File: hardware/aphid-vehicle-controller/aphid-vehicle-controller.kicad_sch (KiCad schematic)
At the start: 0 parts

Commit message: worked on schematic
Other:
- added sheet Analog (analog.kicad_sch)
- added sheet Digital (digital.kicad_sch)
- added sheet Monitor (monitor.kicad_sch)
- sheet CAN ports: added CAN1_MONITOR_RX, CAN1_MONITOR_TX; removed none
- sheet Connectors ports: added ACC1, ACC2, BRAKE, CONTACTOR_LOWER, CONTACTOR_UPPER, HIGH_SIDE_DRIVE, PRECHARGE; removed none
- sheet MCU ports: added LOWER_CONTACTOR_ENABLE, PRECHARGE_ENABLE, UPPER_CONTACTOR_ENABLE; removed none
- sheet Power ports: added VIN_SENSE; removed none

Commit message: more work on pcb
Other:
- added sheet Reset (reset.kicad_sch)
- sheet Analog ports: added IGNITION, IGNITION_FILTERED; removed none
- sheet Connectors ports: added CRANK, IGNITION; removed none
- sheet Digital ports: added CONTACTOR_LOWER, CONTACTOR_UPPER, IGNITION, LOWER_ENABLE, PRECHARGE, PRECHARGE_ENABLE, UPPER_ENABLE; removed none
- sheet Monitor ports: added ACC1_FILTERED, ACC2_FILTERED, ENABLE_RESET; removed none
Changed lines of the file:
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@@
 	)
 	(sheet
-		(at 185.42 82.55)
-		(size 38.1 36.83)
+		(at 185.42 80.01)
+		(size 38.1 21.59)
 		(fields_autoplaced yes)
 		(stroke
@@
 		)
 		(property "Sheetname" "Digital"
-			(at 185.42 81.8384 0)
+			(at 185.42 79.2984 0)
 			(effects
 				(font
@@
 		)
 		(property "Sheetfile" "digital.kicad_sch"
-			(at 185.42 119.9646 0)
+			(at 185.42 102.1846 0)
 			(effects
 				(font
@@
 		)
 		(pin "HIGH_SIDE_SENSE" output
-			(at 185.42 116.84 180)
+			(at 185.42 97.79 180)
 			(effects
 				(font
@@
 		)
 		(pin "HIGH_SIDE_ENABLE" output
-			(at 185.42 114.3 180)
+			(at 185.42 93.98 180)
+			(effects
+				(font
+					(size 1.27 1.27)
+				)
+				(justify left)
+			)
+		)
+		(pin "IGNITION" input
+			(at 223.52 82.55 0)
+			(effects
+				(font
+					(size 1.27 1.27)
+				)
+				(justify right)
+			)
+		)
+		(pin "PRECHARGE" output
+			(at 223.52 87.63 0)
+			(effects
+				(font
+					(size 1.27 1.27)
+				)
+				(justify right)
+			)
+		)
+		(pin "PRECHARGE_ENABLE" input
+			(at 185.42 82.55 180)
+			(effects
+				(font
+					(size 1.27 1.27)
+				)
+				(justify left)
+			)
+		)
+		(pin "CONTACTOR_LOWER" output
+			(at 223.52 92.71 0)
+			(effects
+				(font
+					(size 1.27 1.27)
+				)
+				(justify right)
+			)
+		)
+		(pin "CONTACTOR_UPPER" output
+			(at 223.52 90.17 0)
+			(effects
+				(font
+					(size 1.27 1.27)
+				)
+				(justify right)
+			)
+		)
+		(pin "UPPER_ENABLE" input
+			(at 185.42 85.09 180)
+			(effects
+				(font
+					(size 1.27 1.27)
+				)
+				(justify left)
+			)
+		)
+		(pin "LOWER_ENABLE" input
+			(at 185.42 87.63 180)
 			(effects
 				(font
@@
 				(path "/1bdad060-e59b-443f-afdb-9aa678a43546"
 					(page "8")
+				)
+			)
+		)
+	)
+	(sheet
+		(at 185.42 114.3)
+		(size 38.1 17.78)
+		(fields_autoplaced yes)
+		(stroke
+			(width 0.1524)
+			(type solid)
+		)
+		(fill
+			(color 0 0 0 0.0000)
+		)
+		(property "Sheetname" "Reset"
+			(at 185.42 113.5884 0)
+			(effects
+				(font
+					(size 1.27 1.27)
+				)
+				(justify left bottom)
+			)
+		)
+		(property "Sheetfile" "reset.kicad_sch"
+			(at 185.42 132.6646 0)
+			(effects
+				(font
+					(size 1.27 1.27)
+				)
+				(justify left top)
+			)
+		)
+		(pin "ENABLE_RESET" input
+			(at 185.42 116.84 180)
+			(effects
+				(font
+					(size 1.27 1.27)
+				)
+				(justify left)
+			)
+		)
+		(pin "CRANK" input
+			(at 223.52 116.84 0)
+			(effects
+				(font
+					(size 1.27 1.27)
+				)
+				(justify right)
+			)
+		)
+		(pin "NRST" output
+			(at 185.42 119.38 180)
+			(effects
+				(font
+					(size 1.27 1.27)
+				)
+				(justify left)
+			)
+		)
+		(instances
+			(project "aphid-vehicle-controller"
+				(path "/1bdad060-e59b-443f-afdb-9aa678a43546"
+					(page "9")
 				)
 			)
@@
 	(sheet
 		(at 45.72 33.02)
-		(size 39.37 5.08)
+		(size 39.37 15.875)
 		(fields_autoplaced yes)
 		(stroke
@@
 		)
 		(property "Sheetfile" "power.kicad_sch"
-			(at 45.72 38.6846 0)
+			(at 45.72 49.4796 0)
 			(effects
 				(font
@@
 			)
 		)
+		(pin "IGNITION" output
+			(at 232.41 30.48 180)
+			(effects
+				(font
+					(size 1.27 1.27)
+				)
+				(justify left)
+			)
+		)
+		(pin "CRANK" output
+			(at 232.41 113.03 180)
+			(effects
+				(font
+					(size 1.27 1.27)
+				)
+				(justify left)
+			)
+		)
 		(instances
 			(project "aphid-vehicle-controller"
@@
 			)
 		)
+		(pin "ACC1_FILTERED" input
+			(at 176.53 130.81 0)
+			(effects
+				(font
+					(size 1.27 1.27)
+				)
+				(justify right)
+			)
+		)
+		(pin "ACC2_FILTERED" input
+			(at 176.53 133.35 0)
+			(effects
+				(font
+					(size 1.27 1.27)
+				)
+				(justify right)
+			)
+		)
+		(pin "ENABLE_RESET" output
+			(at 176.53 137.16 0)
+			(effects
+				(font
+					(size 1.27 1.27)
+				)
+				(justify right)
+			)
+		)
 		(instances
 			(project "aphid-vehicle-controller"
@@
 			(effects
 				(font
+					(size 1.27 1.27)
+				)
+				(justify right)
+			)
+		)
+		(pin "IGNITION_FILTERED" output
+			(at 185.42 69.85 180)
+			(effects
+				(font
+					(size 1.27 1.27)
+				)
+				(justify left)
+			)
+		)
+		(pin "IGNITION" input
+			(at 223.52 69.85 0)
+			(effects
+				(font

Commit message: worked on VCM
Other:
- sheet Analog renamed Accelerator
- sheet Digital renamed High Side Out
- removed sheet Reset
- added sheet Brake (brake.kicad_sch)
- added sheet Direction (direction.kicad_sch)
- sheet Accelerator: file analog.kicad_sch -> accelerator.kicad_sch
- sheet Accelerator ports: added none; removed IGNITION, IGNITION_FILTERED
- sheet Connectors ports: added BRAKE1, BRAKE2, DIR_F1, DIR_F2, DIR_R1, DIR_R2, EXT_5V; removed BRAKE, CONTACTOR_LOWER, CONTACTOR_UPPER, PRECHARGE
- sheet High Side Out: file digital.kicad_sch -> hso.kicad_sch
- sheet High Side Out ports: added none; removed CONTACTOR_LOWER, CONTACTOR_UPPER, IGNITION, LOWER_ENABLE, PRECHARGE, PRECHARGE_ENABLE, UPPER_ENABLE
- sheet MCU ports: added ACC, BRAKE, CRANK_SENSE, DIR_F, DIR_R, IGNITION_SENSE, MONITOR_UART_RX, MONITOR_UART_TX, POWER_KEEPALIVE, VIN_SENSE; removed LOWER_CONTACTOR_ENABLE, PRECHARGE_ENABLE, UPPER_CONTACTOR_ENABLE
- sheet Monitor ports: added ACC, BRAKE, CRANK_SENSE, DIR_F, DIR_R, HIGH_SIDE_SENSE, MONITOR_UART_RX, MONITOR_UART_TX; removed ACC1_FILTERED, ACC2_FILTERED, ENABLE_RESET
- sheet Power ports: added CRANK, CRANK_SENSE, EXT_5V, IGNITION, IGNITION_SENSE, POWER_KEEPALIVE; removed none

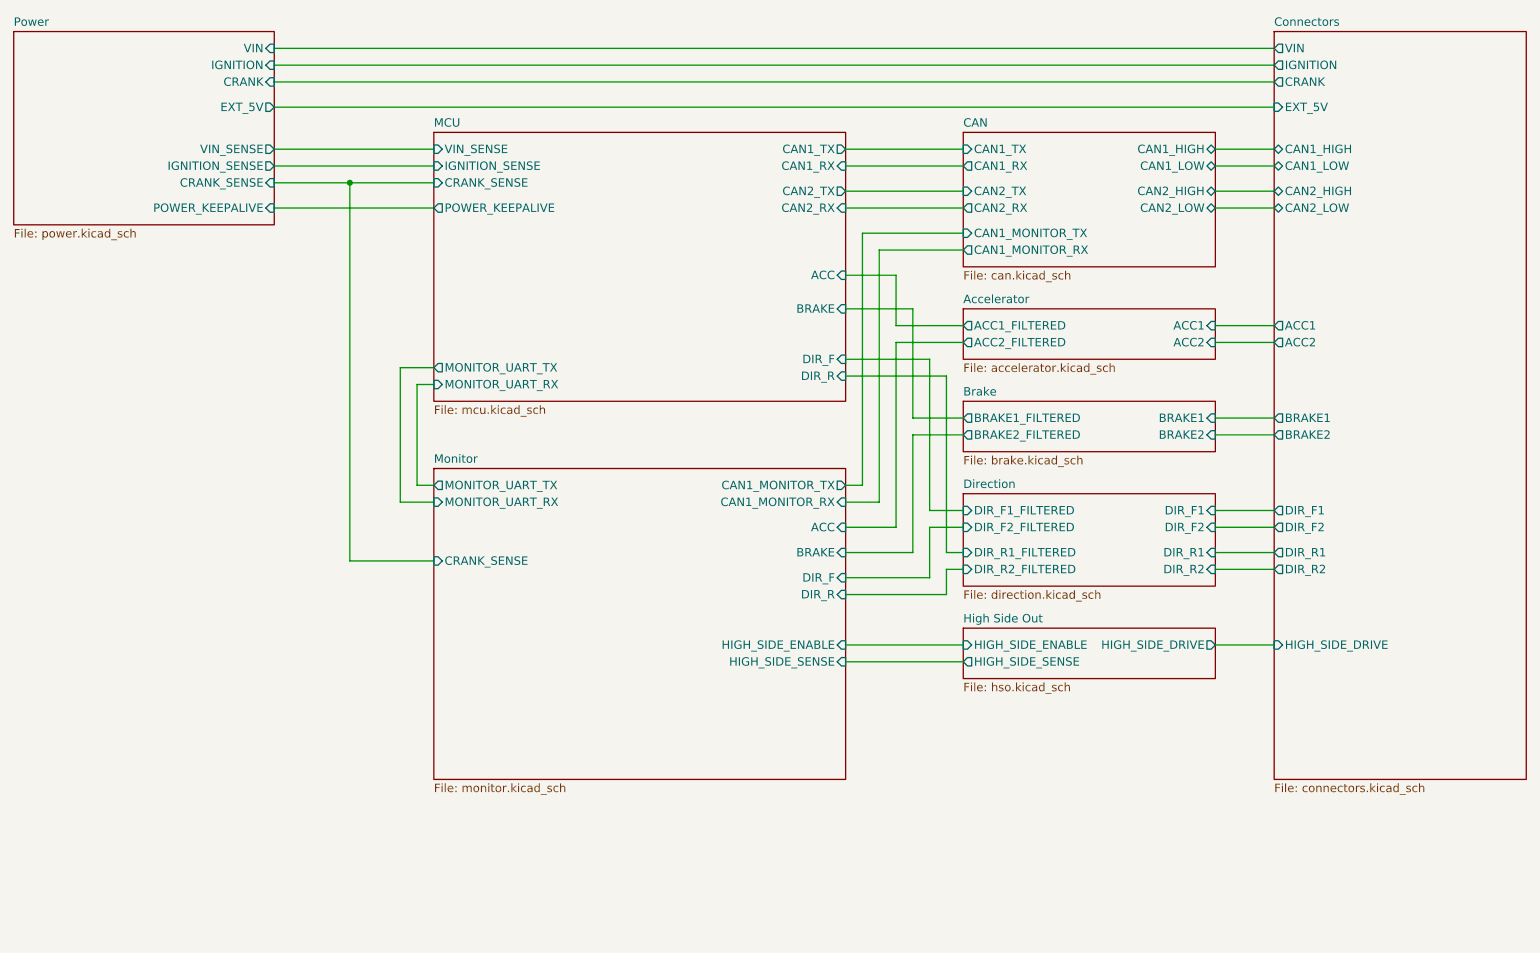
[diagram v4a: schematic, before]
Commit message: feat: changed to STM32G4xx series MCU
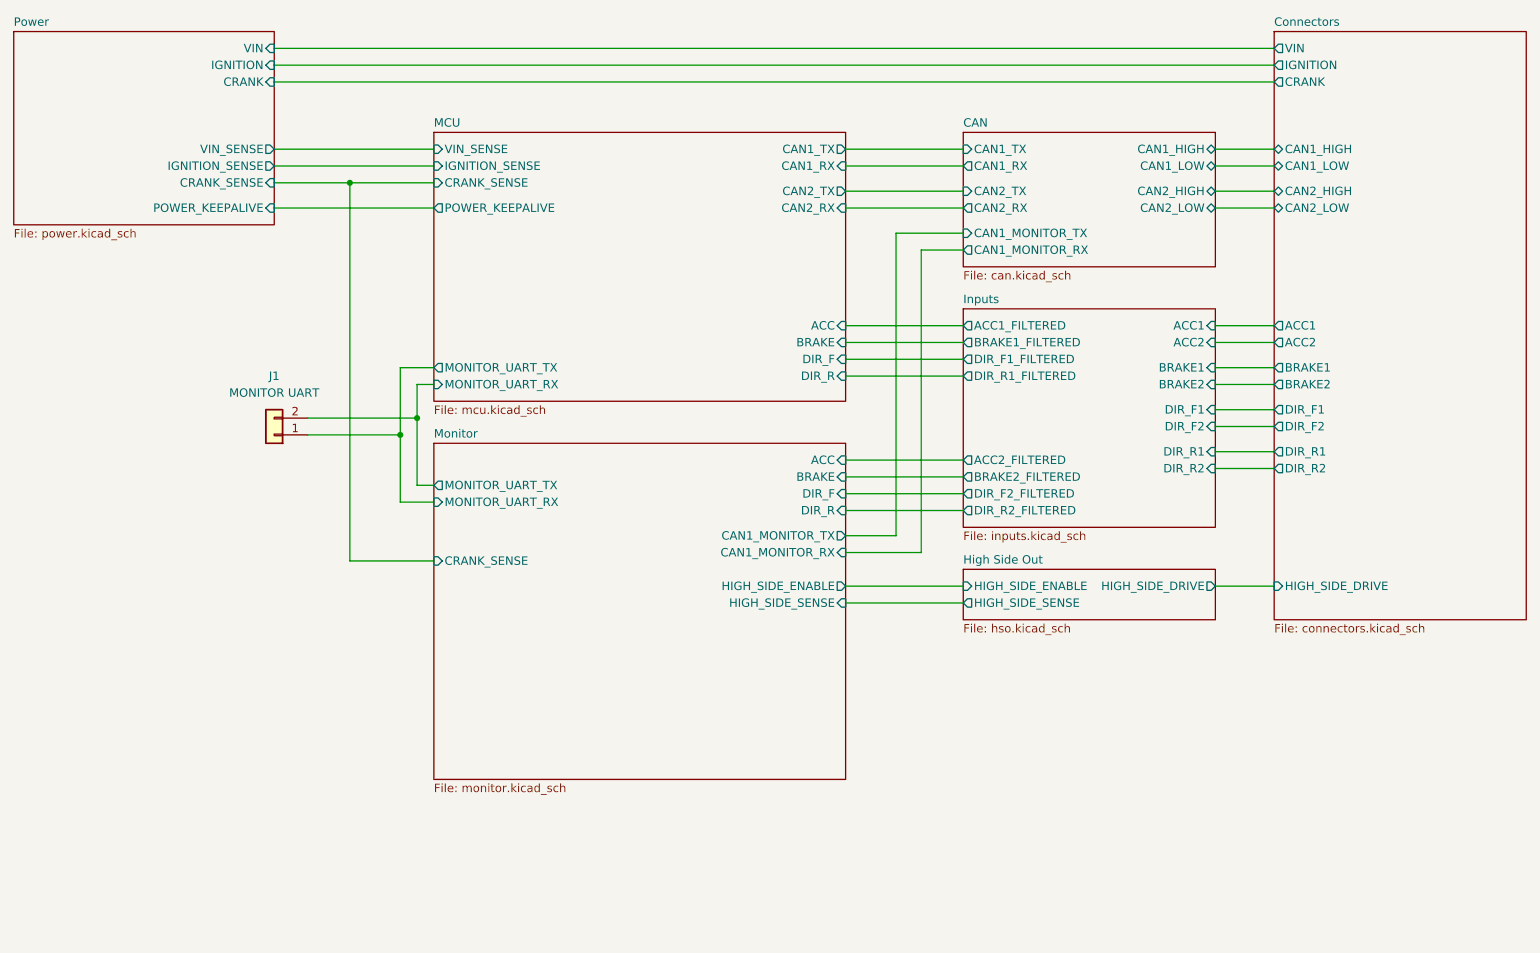
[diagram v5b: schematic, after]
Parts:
- added J1: MONITOR UART, Connector_PinHeader_2.54mm:PinHeader_1x02_P2.54mm_Vertical, symbol Connector_Generic:Conn_01x02
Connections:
- net MCU/MONITOR_UART_RX: now also J1.2 (Pin_2)
- net MCU/MONITOR_UART_TX: now also J1.1 (Pin_1)
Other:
- sheet Accelerator renamed Inputs
- removed sheet Brake
- removed sheet Direction
- sheet Connectors ports: added none; removed EXT_5V
- sheet Inputs: file accelerator.kicad_sch -> inputs.kicad_sch
- sheet Inputs ports: added BRAKE1, BRAKE1_FILTERED, BRAKE2, BRAKE2_FILTERED, DIR_F1, DIR_F1_FILTERED, DIR_F2, DIR_F2_FILTERED, DIR_R1, DIR_R1_FILTERED, DIR_R2, DIR_R2_FILTERED; removed none
- sheet Power ports: added none; removed EXT_5V

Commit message: ERC check passing
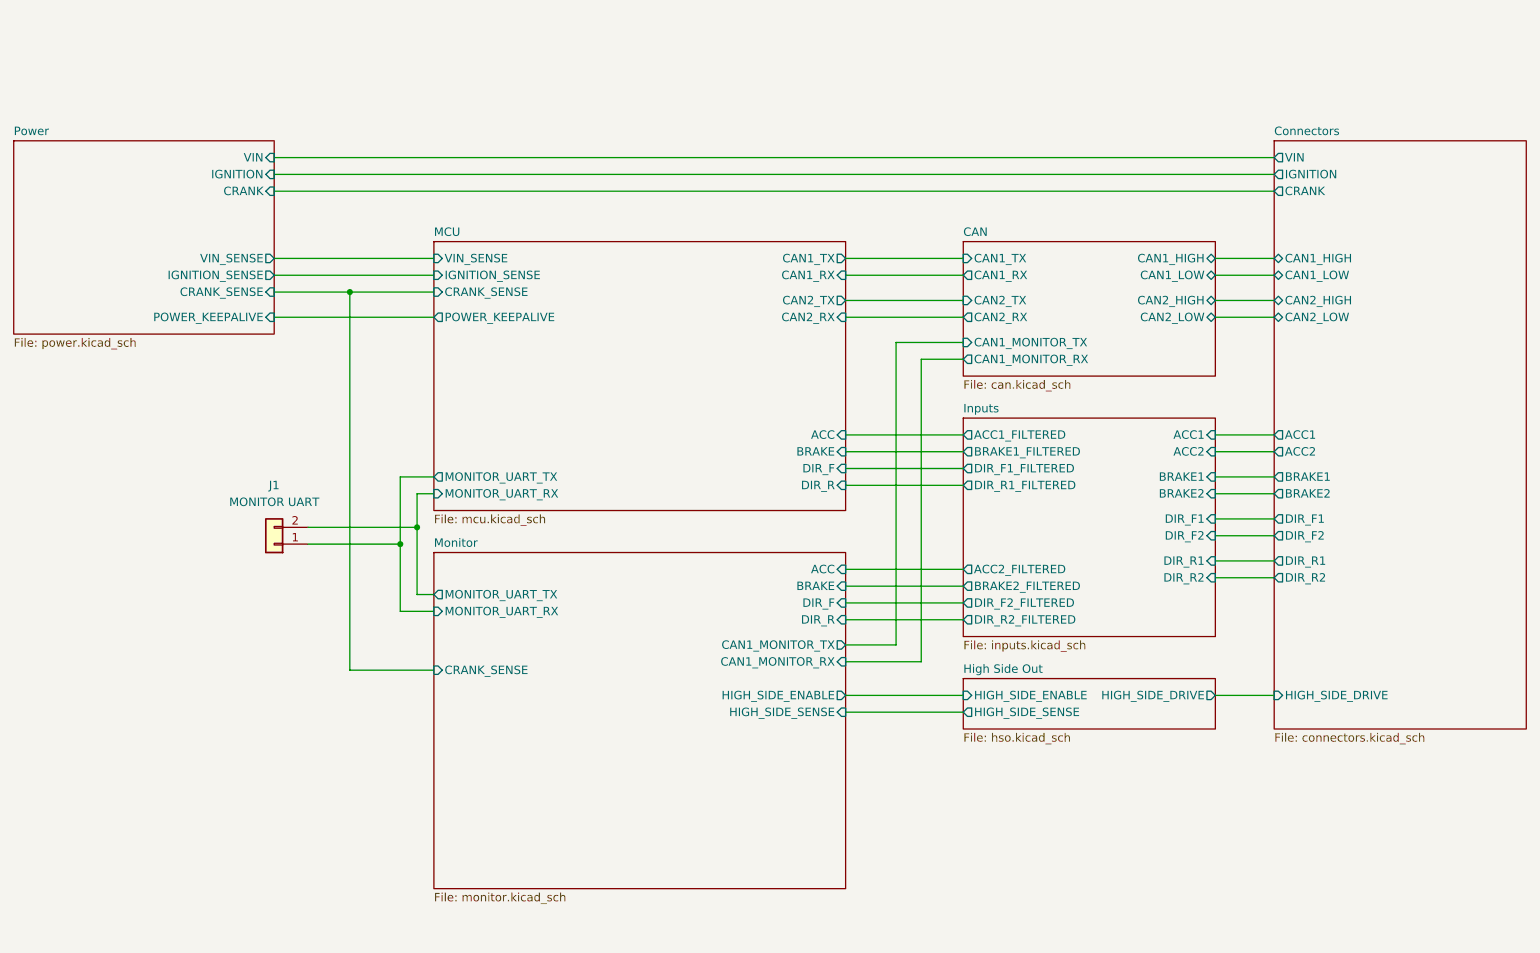
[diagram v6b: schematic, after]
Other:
- moved on the sheet: J1
